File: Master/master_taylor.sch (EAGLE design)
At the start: 46 parts, among them J1 ISP, K1 653002114822, K2 653002114822, K3 653002114822, K4 653002114822, U1 ATMEGA128RFA1, U2 TPS73633-DBVT, U3 ULN2003ADR, Y1 16MHz, Y2 32.768kHz

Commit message: Routed most of VBAT, GND, and 3.3V
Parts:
- removed R4: 0, SparkFun-Passives:RESISTOR0805-RES
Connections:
- removed net MAN_GND: R4.1, U3.5B, U3.6B, U3.7B, U3.E
- net GND: now also U3.5B, U3.6B, U3.7B, U3.E; no longer R4.2
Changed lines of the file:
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@@
 <part name="R3" library="SparkFun-Passives" deviceset="RESISTOR" device="0805-RES" value="10k"/>
 <part name="R10" library="SparkFun-Passives" deviceset="RESISTOR" device="0805-RES" value="10k"/>
-<part name="R4" library="SparkFun-Passives" deviceset="RESISTOR" device="0805-RES" value="0"/>
 </parts>
 <sheets>
@@
 <instance part="R3" gate="G$1" x="-144.78" y="58.42"/>
 <instance part="R10" gate="G$1" x="-149.86" y="53.34"/>
-<instance part="R4" gate="G$1" x="-132.08" y="241.3" rot="R180"/>
 </instances>
 <busses>
@@
 </segment>
 <segment>
-<pinref part="R4" gate="G$1" pin="2"/>
 <wire x1="-137.16" y1="241.3" x2="-137.16" y2="238.76" width="0.1524" layer="91"/>
 <pinref part="GND21" gate="1" pin="GND"/>
 <wire x1="-137.16" y1="238.76" x2="-134.62" y2="238.76" width="0.1524" layer="91"/>
+<wire x1="-128.82" y1="248.44" x2="-127" y2="243.84" width="0.1524" layer="91"/>
+<pinref part="U3" gate="A" pin="E"/>
+<wire x1="-127" y1="243.84" x2="-123.74" y2="243.36" width="0.1524" layer="91"/>
+<pinref part="U3" gate="A" pin="5B"/>
+<wire x1="-123.74" y1="253.52" x2="-128.82" y2="253.52" width="0.1524" layer="91"/>
+<wire x1="-128.82" y1="253.52" x2="-128.82" y2="250.98" width="0.1524" layer="91"/>
+<pinref part="U3" gate="A" pin="6B"/>
+<wire x1="-128.82" y1="250.98" x2="-128.82" y2="248.44" width="0.1524" layer="91"/>
+<wire x1="-123.74" y1="250.98" x2="-128.82" y2="250.98" width="0.1524" layer="91"/>
+<pinref part="U3" gate="A" pin="7B"/>
+<wire x1="-123.74" y1="248.44" x2="-128.82" y2="248.44" width="0.1524" layer="91"/>
+<junction x="-128.82" y="250.98"/>
+<junction x="-128.82" y="248.44"/>
+<wire x1="-127" y1="243.84" x2="-127" y2="241.3" width="0.1524" layer="91"/>
+<wire x1="-127" y1="241.3" x2="-137.16" y2="241.3" width="0.1524" layer="91"/>
 </segment>
 </net>
@@
 </segment>
 </net>
-<net name="MAN_GND" class="0">
-<segment>
-<wire x1="-128.82" y1="248.44" x2="-127" y2="243.84" width="0.1524" layer="91"/>
-<pinref part="U3" gate="A" pin="E"/>
-<wire x1="-127" y1="243.84" x2="-123.74" y2="243.36" width="0.1524" layer="91"/>
-<pinref part="U3" gate="A" pin="5B"/>
-<wire x1="-123.74" y1="253.52" x2="-128.82" y2="253.52" width="0.1524" layer="91"/>
-<wire x1="-128.82" y1="253.52" x2="-128.82" y2="250.98" width="0.1524" layer="91"/>
-<pinref part="U3" gate="A" pin="6B"/>
-<wire x1="-128.82" y1="250.98" x2="-128.82" y2="248.44" width="0.1524" layer="91"/>
-<wire x1="-123.74" y1="250.98" x2="-128.82" y2="250.98" width="0.1524" layer="91"/>
-<pinref part="U3" gate="A" pin="7B"/>
-<wire x1="-123.74" y1="248.44" x2="-128.82" y2="248.44" width="0.1524" layer="91"/>
-<junction x="-128.82" y="250.98"/>
-<junction x="-128.82" y="248.44"/>
-<pinref part="R4" gate="G$1" pin="1"/>
-<wire x1="-127" y1="243.84" x2="-127" y2="241.3" width="0.1524" layer="91"/>
-</segment>
-</net>

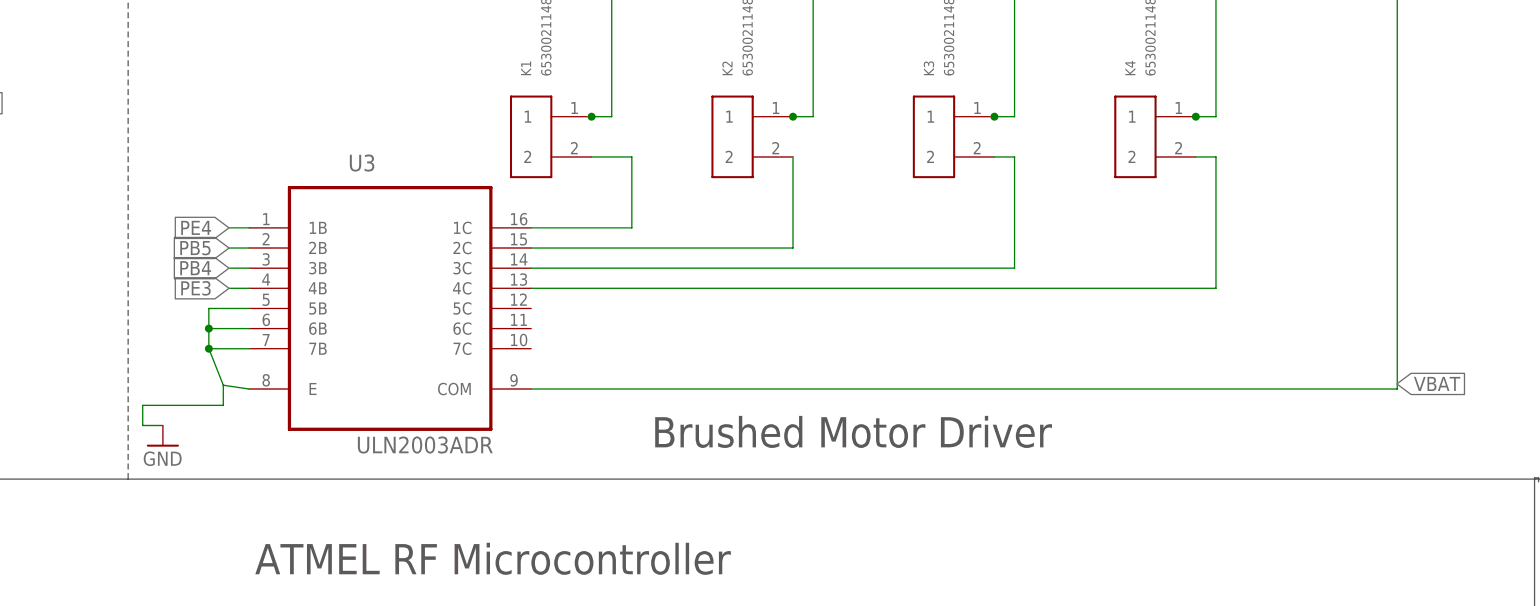
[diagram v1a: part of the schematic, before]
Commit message: Routing is almost there...
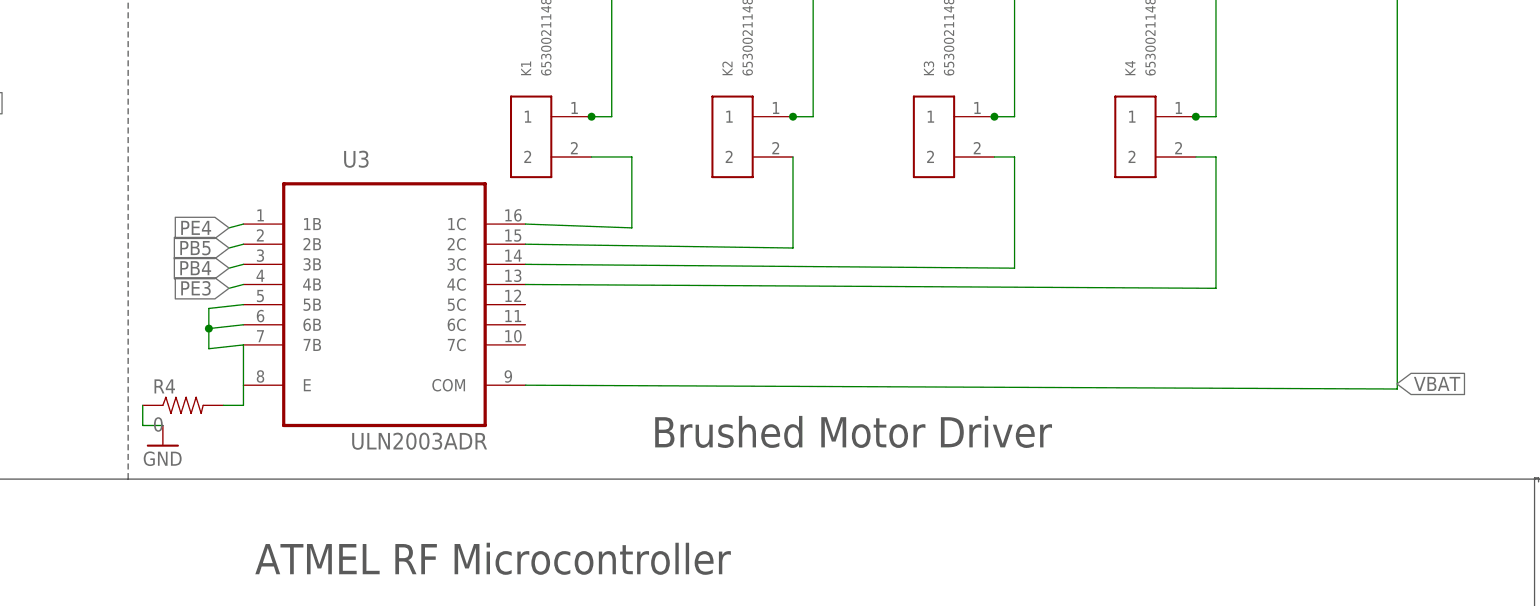
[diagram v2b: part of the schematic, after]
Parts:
- added R4: 0, SparkFun-Passives:RESISTOR0805-RES
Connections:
- new net N$12: R4.2, U3.5B, U3.6B, U3.7B, U3.E
- net GND: now also R4.1; no longer U3.5B, U3.6B, U3.7B, U3.E
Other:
- moved on the sheet: U3
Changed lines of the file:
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@@
 <part name="R3" library="SparkFun-Passives" deviceset="RESISTOR" device="0805-RES" value="10k"/>
 <part name="R10" library="SparkFun-Passives" deviceset="RESISTOR" device="0805-RES" value="10k"/>
+<part name="R4" library="SparkFun-Passives" deviceset="RESISTOR" device="0805-RES" value="0"/>
 </parts>
 <sheets>
@@
 <attribute name="MPN" x="-11.98" y="275.16" size="1.778" layer="96" display="off"/>
 </instance>
-<instance part="U3" gate="A" x="-105.96" y="256.06"/>
+<instance part="U3" gate="A" x="-106.68" y="256.54"/>
 <instance part="GND21" gate="1" x="-134.62" y="236.22"/>
 <instance part="JP3" gate="G$1" x="-269.24" y="276.86"/>
@@
 <instance part="R3" gate="G$1" x="-144.78" y="58.42"/>
 <instance part="R10" gate="G$1" x="-149.86" y="53.34"/>
+<instance part="R4" gate="G$1" x="-132.08" y="241.3"/>
 </instances>
 <busses>
@@
 </segment>
 <segment>
+<pinref part="GND21" gate="1" pin="GND"/>
 <wire x1="-137.16" y1="241.3" x2="-137.16" y2="238.76" width="0.1524" layer="91"/>
-<pinref part="GND21" gate="1" pin="GND"/>
 <wire x1="-137.16" y1="238.76" x2="-134.62" y2="238.76" width="0.1524" layer="91"/>
-<wire x1="-128.82" y1="248.44" x2="-127" y2="243.84" width="0.1524" layer="91"/>
-<pinref part="U3" gate="A" pin="E"/>
-<wire x1="-127" y1="243.84" x2="-123.74" y2="243.36" width="0.1524" layer="91"/>
-<pinref part="U3" gate="A" pin="5B"/>
-<wire x1="-123.74" y1="253.52" x2="-128.82" y2="253.52" width="0.1524" layer="91"/>
-<wire x1="-128.82" y1="253.52" x2="-128.82" y2="250.98" width="0.1524" layer="91"/>
-<pinref part="U3" gate="A" pin="6B"/>
-<wire x1="-128.82" y1="250.98" x2="-128.82" y2="248.44" width="0.1524" layer="91"/>
-<wire x1="-123.74" y1="250.98" x2="-128.82" y2="250.98" width="0.1524" layer="91"/>
-<pinref part="U3" gate="A" pin="7B"/>
-<wire x1="-123.74" y1="248.44" x2="-128.82" y2="248.44" width="0.1524" layer="91"/>
-<junction x="-128.82" y="250.98"/>
-<junction x="-128.82" y="248.44"/>
-<wire x1="-127" y1="243.84" x2="-127" y2="241.3" width="0.1524" layer="91"/>
-<wire x1="-127" y1="241.3" x2="-137.16" y2="241.3" width="0.1524" layer="91"/>
+<pinref part="R4" gate="G$1" pin="1"/>
 </segment>
 </net>
@@
 <segment>
 <pinref part="U3" gate="A" pin="1B"/>
-<wire x1="-123.74" y1="263.68" x2="-126.28" y2="263.68" width="0.1524" layer="91"/>
+<wire x1="-124.46" y1="264.16" x2="-126.28" y2="263.68" width="0.1524" layer="91"/>
 <label x="-126.28" y="263.68" size="1.778" layer="95" rot="R180" xref="yes"/>
 </segment>
@@
 <segment>
 <pinref part="U3" gate="A" pin="4B"/>
-<wire x1="-123.74" y1="256.06" x2="-126.28" y2="256.06" width="0.1524" layer="91"/>
+<wire x1="-124.46" y1="256.54" x2="-126.28" y2="256.06" width="0.1524" layer="91"/>
 <label x="-126.28" y="256.06" size="1.778" layer="95" rot="R180" xref="yes"/>
 </segment>
@@
 <segment>
 <pinref part="U3" gate="A" pin="2B"/>
-<wire x1="-123.74" y1="261.14" x2="-126.28" y2="261.14" width="0.1524" layer="91"/>
+<wire x1="-124.46" y1="261.62" x2="-126.28" y2="261.14" width="0.1524" layer="91"/>
 <label x="-126.28" y="261.14" size="1.778" layer="95" rot="R180" xref="yes"/>
 </segment>
@@
 <segment>
 <pinref part="U3" gate="A" pin="3B"/>
-<wire x1="-123.74" y1="258.6" x2="-126.28" y2="258.6" width="0.1524" layer="91"/>
+<wire x1="-124.46" y1="259.08" x2="-126.28" y2="258.6" width="0.1524" layer="91"/>
 <label x="-126.28" y="258.6" size="1.778" layer="95" rot="R180" xref="yes"/>
 </segment>
@@
 <segment>
 <pinref part="U3" gate="A" pin="1C"/>
-<wire x1="-88.18" y1="263.68" x2="-75.48" y2="263.68" width="0.1524" layer="91"/>
+<wire x1="-88.9" y1="264.16" x2="-75.48" y2="263.68" width="0.1524" layer="91"/>
 <wire x1="-75.48" y1="263.68" x2="-75.48" y2="272.62" width="0.1524" layer="91"/>
 <pinref part="K1" gate="G$1" pin="2"/>
@@
 <pinref part="U3" gate="A" pin="2C"/>
 <pinref part="K2" gate="G$1" pin="2"/>
-<wire x1="-88.18" y1="261.14" x2="-55.16" y2="261.14" width="0.1524" layer="91"/>
+<wire x1="-88.9" y1="261.62" x2="-55.16" y2="261.14" width="0.1524" layer="91"/>
 <wire x1="-55.16" y1="261.14" x2="-55.16" y2="272.62" width="0.1524" layer="91"/>
 </segment>
@@
 <segment>
 <pinref part="U3" gate="A" pin="3C"/>
-<wire x1="-88.18" y1="258.6" x2="-27.22" y2="258.6" width="0.1524" layer="91"/>
+<wire x1="-88.9" y1="259.08" x2="-27.22" y2="258.6" width="0.1524" layer="91"/>
 <wire x1="-27.22" y1="258.6" x2="-27.22" y2="272.62" width="0.1524" layer="91"/>
 <pinref part="K3" gate="G$1" pin="2"/>
@@
 <segment>
 <pinref part="U3" gate="A" pin="4C"/>
-<wire x1="-88.18" y1="256.06" x2="-1.82" y2="256.06" width="0.1524" layer="91"/>
+<wire x1="-88.9" y1="256.54" x2="-1.82" y2="256.06" width="0.1524" layer="91"/>
 <wire x1="-1.82" y1="256.06" x2="-1.82" y2="272.62" width="0.1524" layer="91"/>
 <pinref part="K4" gate="G$1" pin="2"/>
@@
 <segment>
 <pinref part="U3" gate="A" pin="COM"/>
-<wire x1="-88.18" y1="243.36" x2="21.04" y2="243.36" width="0.1524" layer="91"/>
+<wire x1="-88.9" y1="243.84" x2="21.04" y2="243.36" width="0.1524" layer="91"/>
 <wire x1="21.04" y1="243.36" x2="21.04" y2="292.94" width="0.1524" layer="91"/>
 <wire x1="21.04" y1="292.94" x2="-1.82" y2="292.94" width="0.1524" layer="91"/>
@@
 </segment>
 </net>
+<net name="N$12" class="0">
+<segment>
+<pinref part="R4" gate="G$1" pin="2"/>
+<wire x1="-127" y1="241.3" x2="-124.46" y2="241.3" width="0.1524" layer="91"/>
+<pinref part="U3" gate="A" pin="5B"/>
+<wire x1="-124.46" y1="254" x2="-128.82" y2="253.52" width="0.1524" layer="91"/>
+<wire x1="-128.82" y1="253.52" x2="-128.82" y2="250.98" width="0.1524" layer="91"/>
+<pinref part="U3" gate="A" pin="6B"/>
+<wire x1="-128.82" y1="250.98" x2="-128.82" y2="248.44" width="0.1524" layer="91"/>
+<wire x1="-124.46" y1="251.46" x2="-128.82" y2="250.98" width="0.1524" layer="91"/>
+<pinref part="U3" gate="A" pin="7B"/>
+<wire x1="-124.46" y1="248.92" x2="-128.82" y2="248.44" width="0.1524" layer="91"/>
+<junction x="-128.82" y="250.98"/>
+<pinref part="U3" gate="A" pin="E"/>
+<wire x1="-124.46" y1="243.84" x2="-124.46" y2="248.92" width="0.1524" layer="91"/>
+<wire x1="-124.46" y1="241.3" x2="-124.46" y2="243.84" width="0.1524" layer="91"/>
+</segment>
+</net>

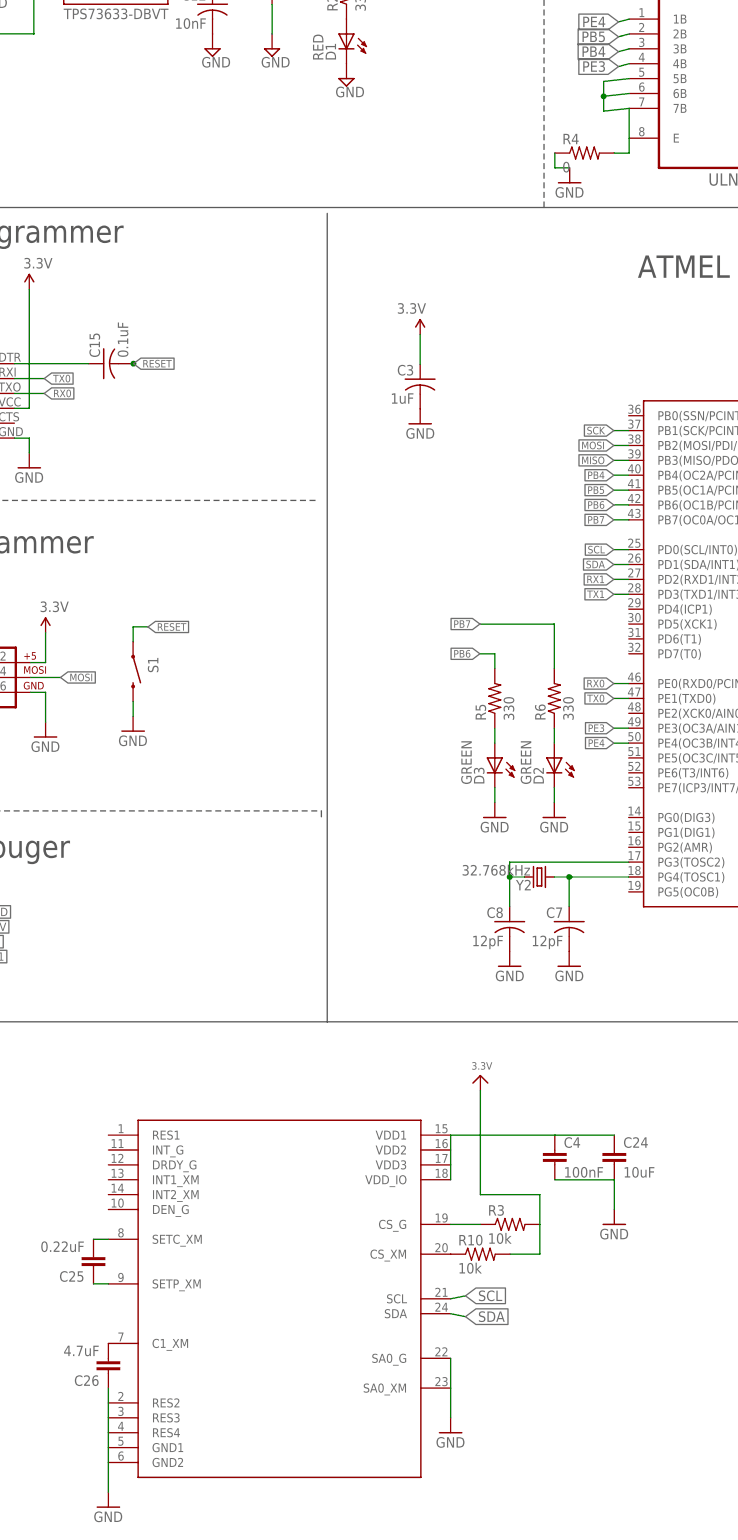
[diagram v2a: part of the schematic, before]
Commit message: Fixed some minor ERC errors
Adjusted wing fins.
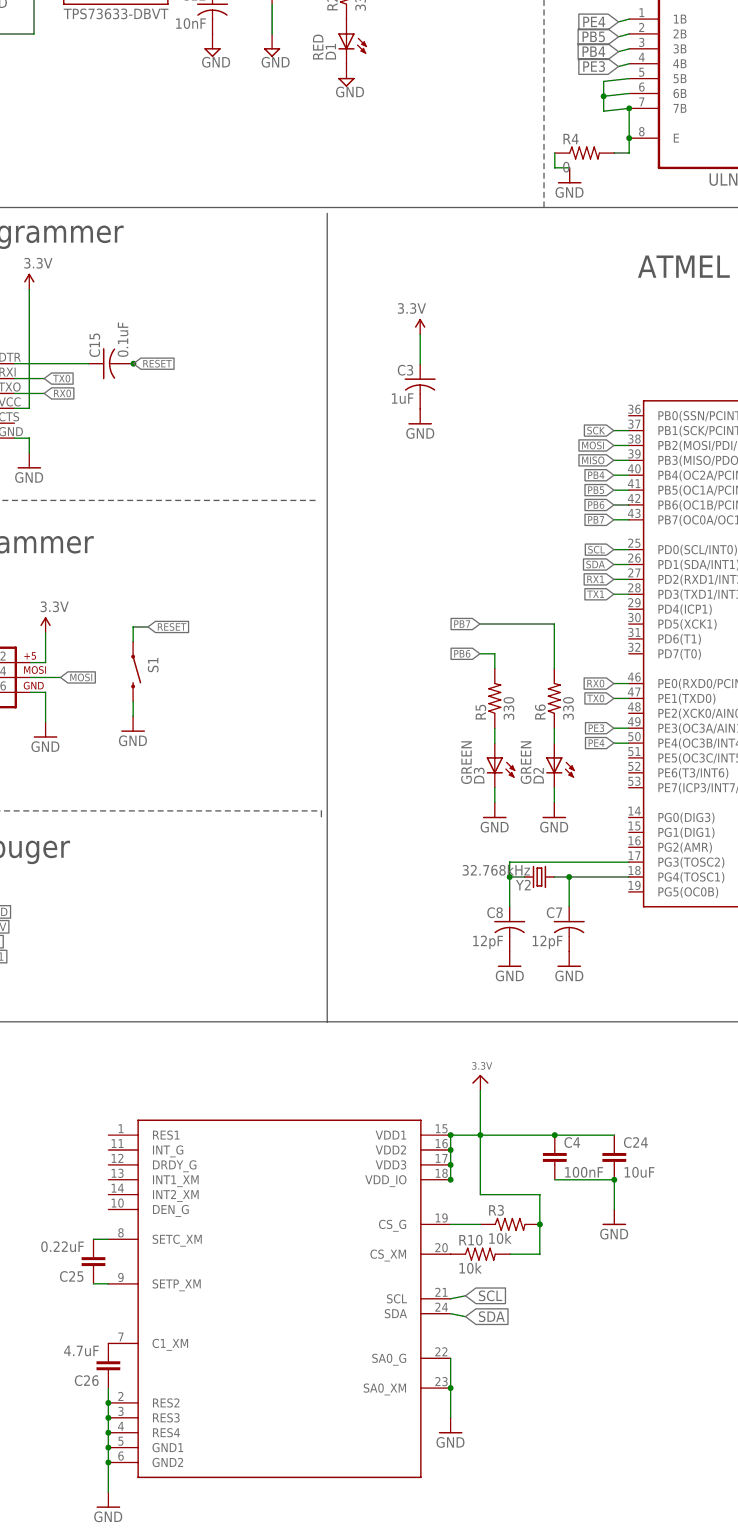
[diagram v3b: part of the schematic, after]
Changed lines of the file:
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@@
 <pinref part="GND22" gate="1" pin="GND"/>
 <wire x1="-127" y1="66.04" x2="-127" y2="60.96" width="0.1524" layer="91"/>
+<junction x="-127" y="66.04"/>
 </segment>
 <segment>
@@
 <pinref part="GND5" gate="1" pin="GND"/>
 <wire x1="-213.36" y1="17.78" x2="-213.36" y2="12.7" width="0.1524" layer="91"/>
+<junction x="-213.36" y="27.94"/>
+<junction x="-213.36" y="25.4"/>
+<junction x="-213.36" y="22.86"/>
+<junction x="-213.36" y="20.32"/>
+<junction x="-213.36" y="17.78"/>
 </segment>
 <segment>
@@
 <pinref part="GND23" gate="1" pin="GND"/>
 <wire x1="-154.94" y1="30.48" x2="-154.94" y2="25.4" width="0.1524" layer="91"/>
+<junction x="-154.94" y="30.48"/>
 </segment>
 <segment>
@@
 <wire x1="-139.7" y1="63.5" x2="-149.86" y2="63.5" width="0.1524" layer="91"/>
 <wire x1="-149.86" y1="63.5" x2="-149.86" y2="73.66" width="0.1524" layer="91"/>
+<junction x="-137.16" y="73.66"/>
+<junction x="-154.94" y="73.66"/>
+<junction x="-149.86" y="73.66"/>
+<junction x="-154.94" y="71.12"/>
+<junction x="-154.94" y="68.58"/>
+<junction x="-154.94" y="66.04"/>
+<junction x="-139.7" y="58.42"/>
 </segment>
 </net>
@@
 <wire x1="-124.46" y1="243.84" x2="-124.46" y2="248.92" width="0.1524" layer="91"/>
 <wire x1="-124.46" y1="241.3" x2="-124.46" y2="243.84" width="0.1524" layer="91"/>
+<junction x="-124.46" y="243.84"/>
+<junction x="-124.46" y="248.92"/>
 </segment>
 </net>
@@
 </sheet>
 </sheets>
+<errors>
+</errors>
 </schematic>
 </drawing>
